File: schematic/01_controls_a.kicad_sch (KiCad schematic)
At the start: 19 parts, among them SW101 C, SW102 C sharp, SW103 D, SW104 D sharp, SW105 E, SW106 F, U401 74HC14

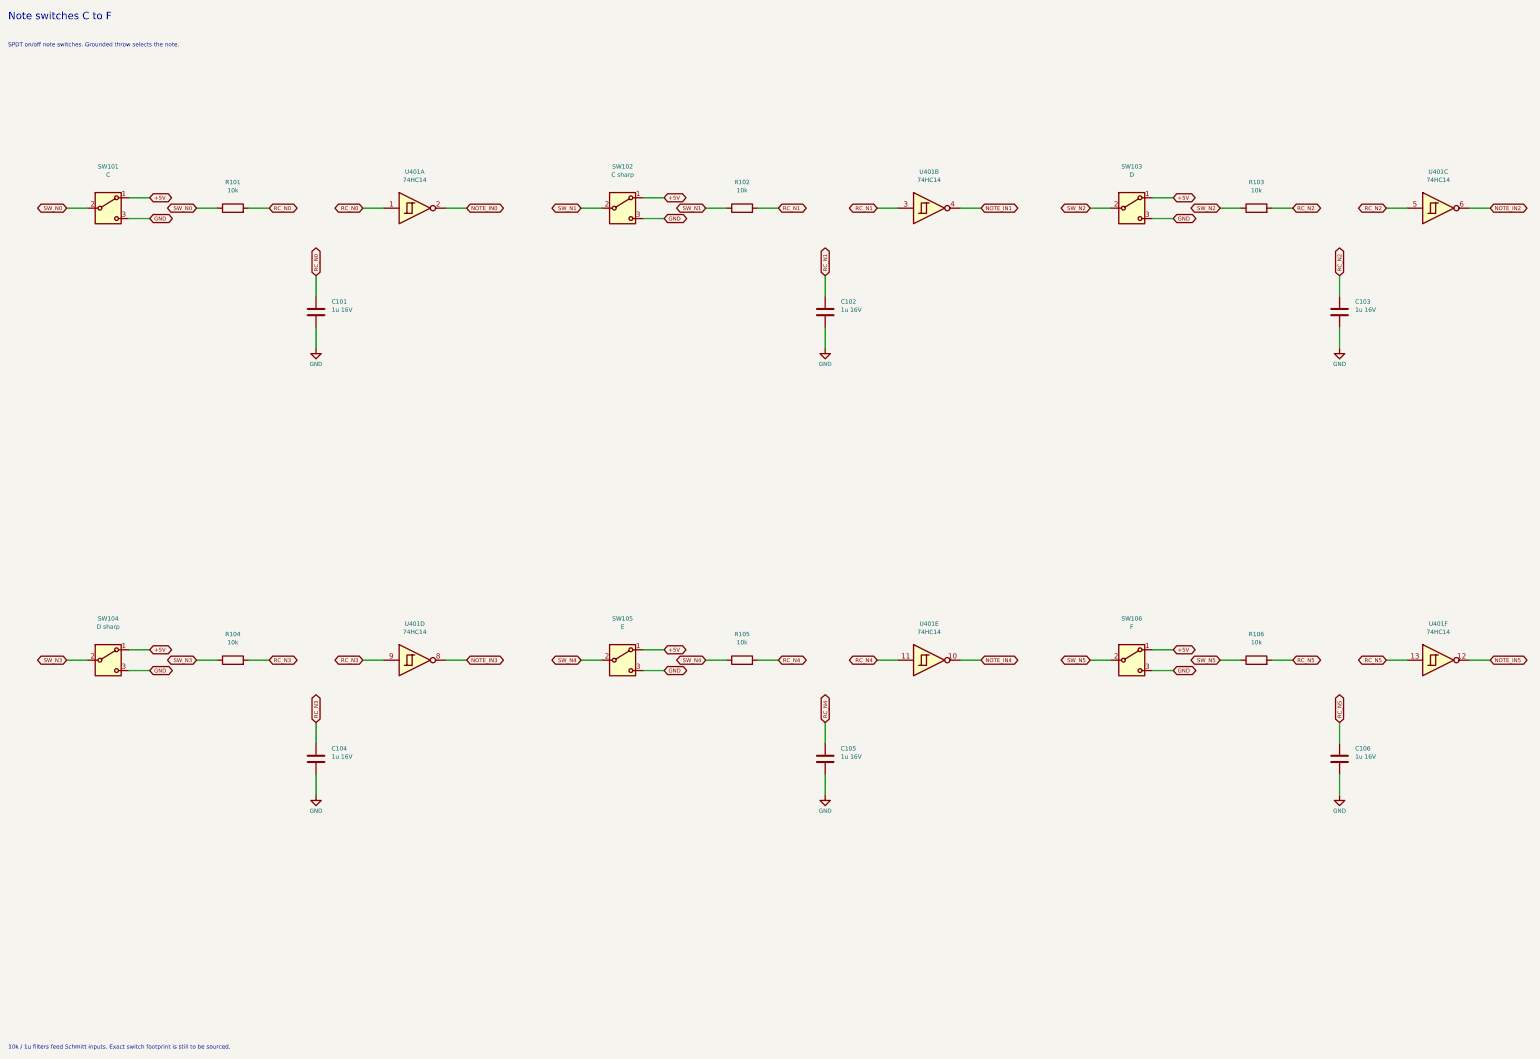
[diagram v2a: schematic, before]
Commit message: pick controls and start pcb placement
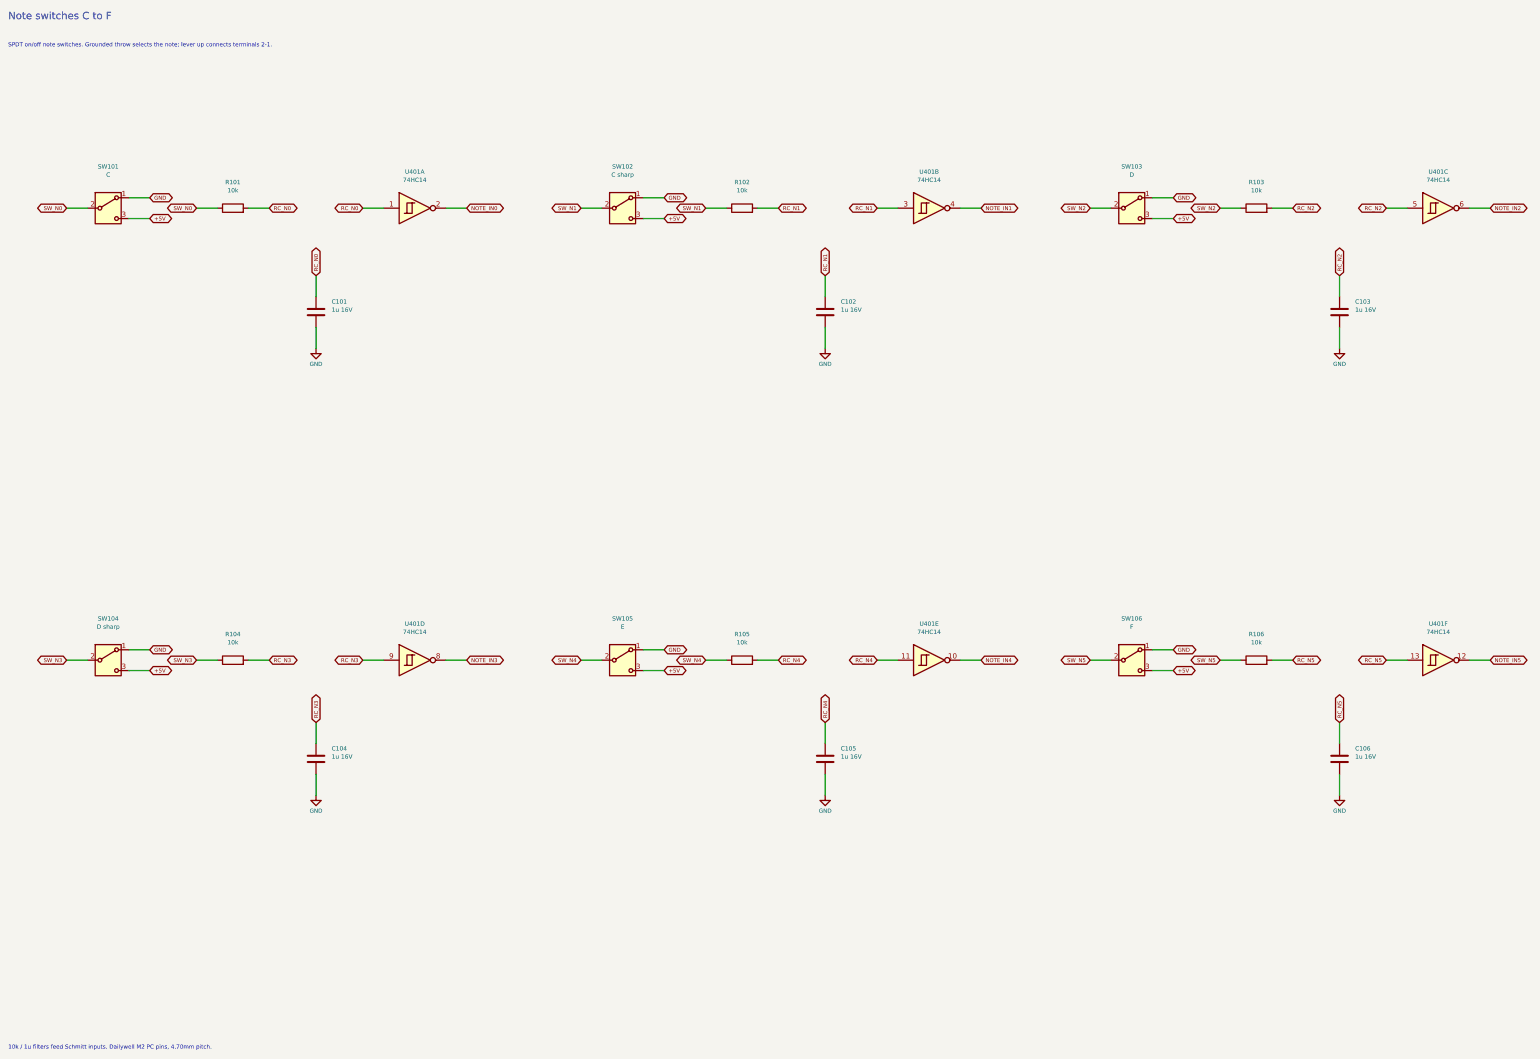
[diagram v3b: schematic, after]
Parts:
- SW101, SW102, SW103, SW104, SW105, SW106: footprint (none) -> Arpeggiator:SW_Dailywell_1M_SPDT_M2; MPN (none) -> 1MS1T1B1M2QES; Manufacturer (none) -> Dailywell; Supplier (none) -> Tayda; Supplier URL (none) -> https://www.taydaelectronics.com/electromechanical/switches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
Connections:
- net +5V: now also SW101.3 (C), SW102.3 (C), SW103.3 (C), SW104.3 (C), SW105.3 (C), SW106.3 (C); no longer SW101.1 (A), SW102.1 (A), SW103.1 (A), SW104.1 (A), SW105.1 (A), SW106.1 (A)
- net GND: now also SW101.1 (A), SW102.1 (A), SW103.1 (A), SW104.1 (A), SW105.1 (A), SW106.1 (A); no longer SW101.3 (C), SW102.3 (C), SW103.3 (C), SW104.3 (C), SW105.3 (C), SW106.3 (C)
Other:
- note added: "10k / 1u filters feed Schmitt inputs. Dailywell M2 PC pins, 4.70mm pitch."
- note added: "SPDT on/off note switches. Grounded throw selects the note; lever up connects terminals 2-1."
- note removed: "10k / 1u filters feed Schmitt inputs. Exact switch footprint is still to be sourced."
- note removed: "SPDT on/off note switches. Grounded throw selects the note."
